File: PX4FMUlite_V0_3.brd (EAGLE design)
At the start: 48.6 x 34.9 mm, 151 parts, among them J2 DF13-4P-1.25V, J201 DF13C-6P-1.25V, J202 DF13C-6P-1.25V, J203 DF13C-6P-1.25V, J3 DF13C-4P-1.25V, J302 DF13C-4P-1.25V, J401 DF13C-4P-1.25V, J403 DF13C-7P-1.25V, J405 DF13C-4P-1.25V, J801 JST-ZH-3, J802 DF13C-3P-1.25V, M3_MOUNT1101 MOUNT-HOLE3.1MM, M3_MOUNT1102 MOUNT-HOLE3.1MM, M3_MOUNT1103 MOUNT-HOLE3.1MM, M3_MOUNT1104 MOUNT-HOLE3.1MM, U101 STM32F4X7VX, U2 MAX3051, U401 MAX3051, U903 74LVC2G240, X101 3.2x2.5 mm / 24 MHz / 15 ppm

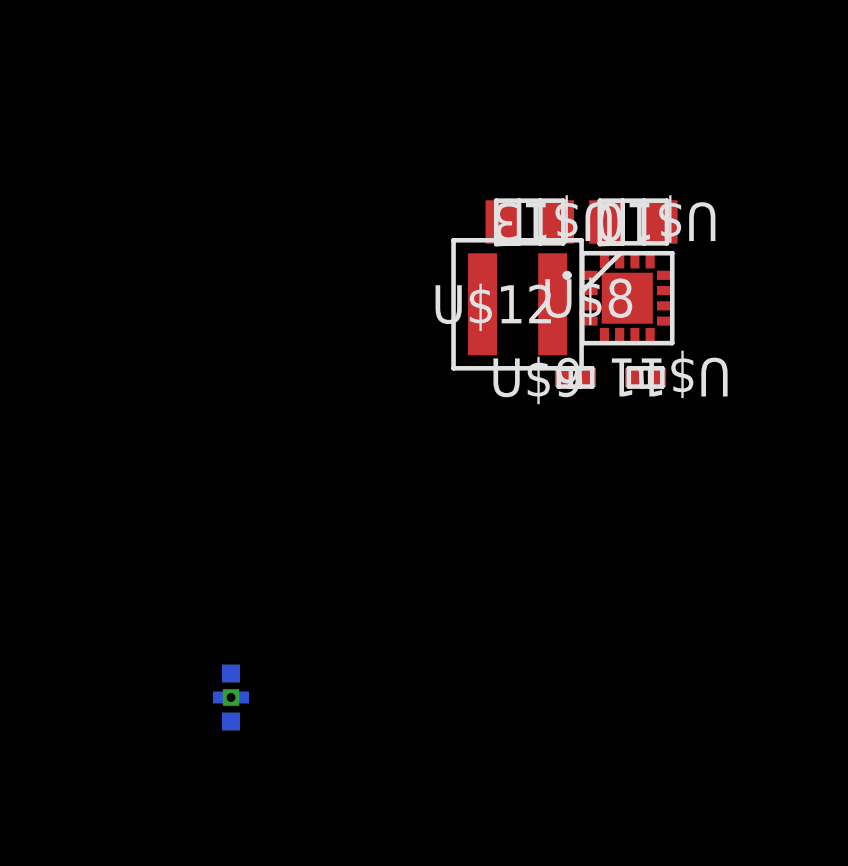
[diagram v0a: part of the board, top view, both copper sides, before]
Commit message: Added cap to TPS63031 buck-boost
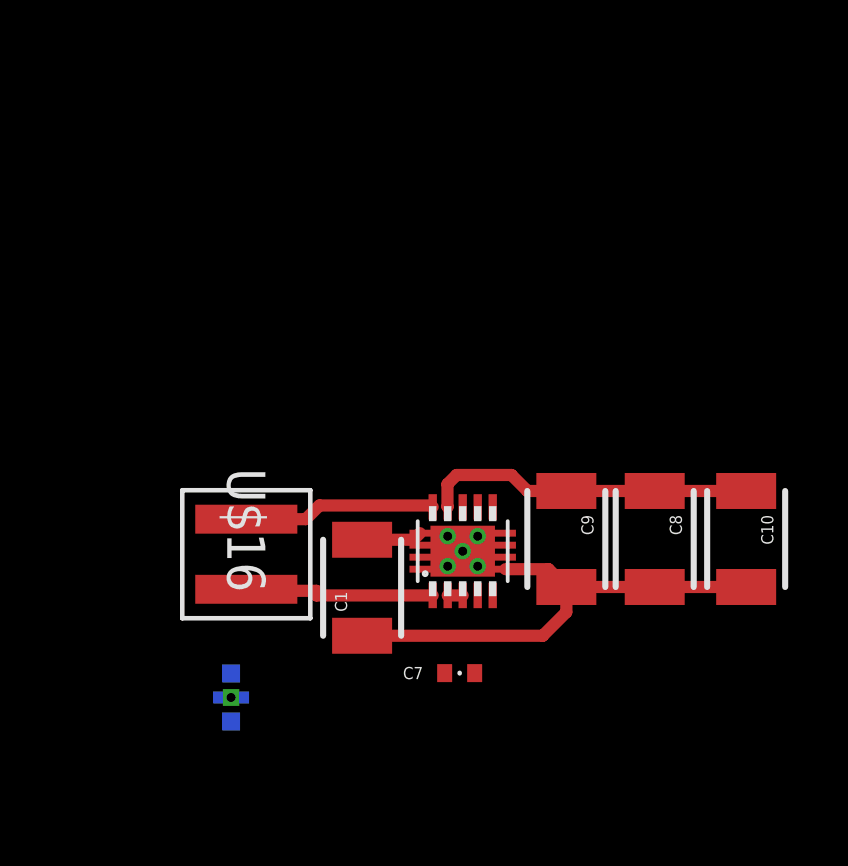
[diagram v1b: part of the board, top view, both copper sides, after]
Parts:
- removed U$10: GRM21BR61C106KE15L, ti_tps_soln2:0805
- removed U$11: GRM155R61C223KA01D, ti_tps_soln2:0402
- removed U$12: XFL4020-222MEB, ti_tps_soln2:XFL4020
- removed U$13: LMK212BJ226MG-T, ti_tps_soln2:0805
- removed U$8: TPS62143RGTR, ti_tps_soln2:S-PVQFN-N16
- removed U$9: CRCW0402100KFKED, ti_tps_soln2:0402
- added C1, C10, C8, C9: 22uF, SparkFun-Capacitors:1210
- added C7: 8p, pixhawk2:0402-CAP
- added U$15: TPS6303X, PX4lite:PWSON10
- added U$16: XFL4020-222MEB, ti_tps_soln2:XFL4020
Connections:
- removed net N$40: U$11.1, U$8.9
- new net N$10: U$15.14, U$16.1
- new net N$17: U$15.1, U$16.2
- new net VOUT: C10.1, C8.1, C9.1, U$15.13
- net !VDD_SERVO_VALID: no longer U$8.4, U$9.2
- net GND: now also U$15.11; no longer U$10.2, U$11.2, U$13.1, U$8.15, U$8.17, U$8.5, U$8.6, U$8.7, U$8.8
- net N$14: now also C1.2, C10.2, C8.2, C9.2, U$15.15, U$15.16, U$15.17, U$15.18, U$15.19, U$15.20, U$15.21, U$15.22, U$15.23, U$15.6, U$15.7, U$15.8, U$15.9, U$15.EP; no longer U$12.2, U$8.1
- net VDD_5V_IN: no longer U$12.1, U$13.2, U$8.14, U$9.1
- net VDD_IN: now also C1.1, U$15.2, U$15.3; no longer U$10.1, U$8.10, U$8.11, U$8.13
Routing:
- net N$14: track 0.00 -> 13.1 mm
- net VOUT: track 0.00 -> 11.1 mm
- net VDD_IN: track 0.00 -> 8.65 mm
- net N$10: track 0.00 -> 6.42 mm
- net N$17: track 0.00 -> 6.42 mm

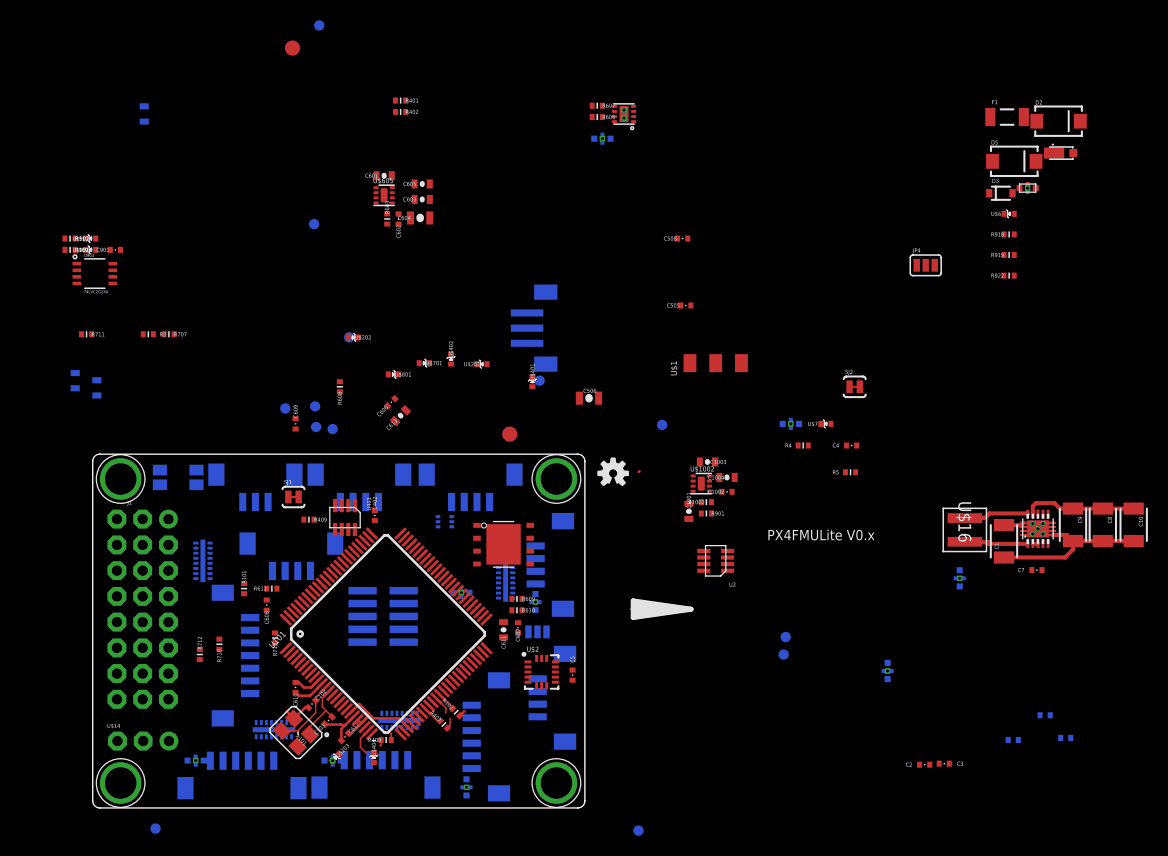
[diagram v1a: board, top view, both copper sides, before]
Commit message: Crystal rewire
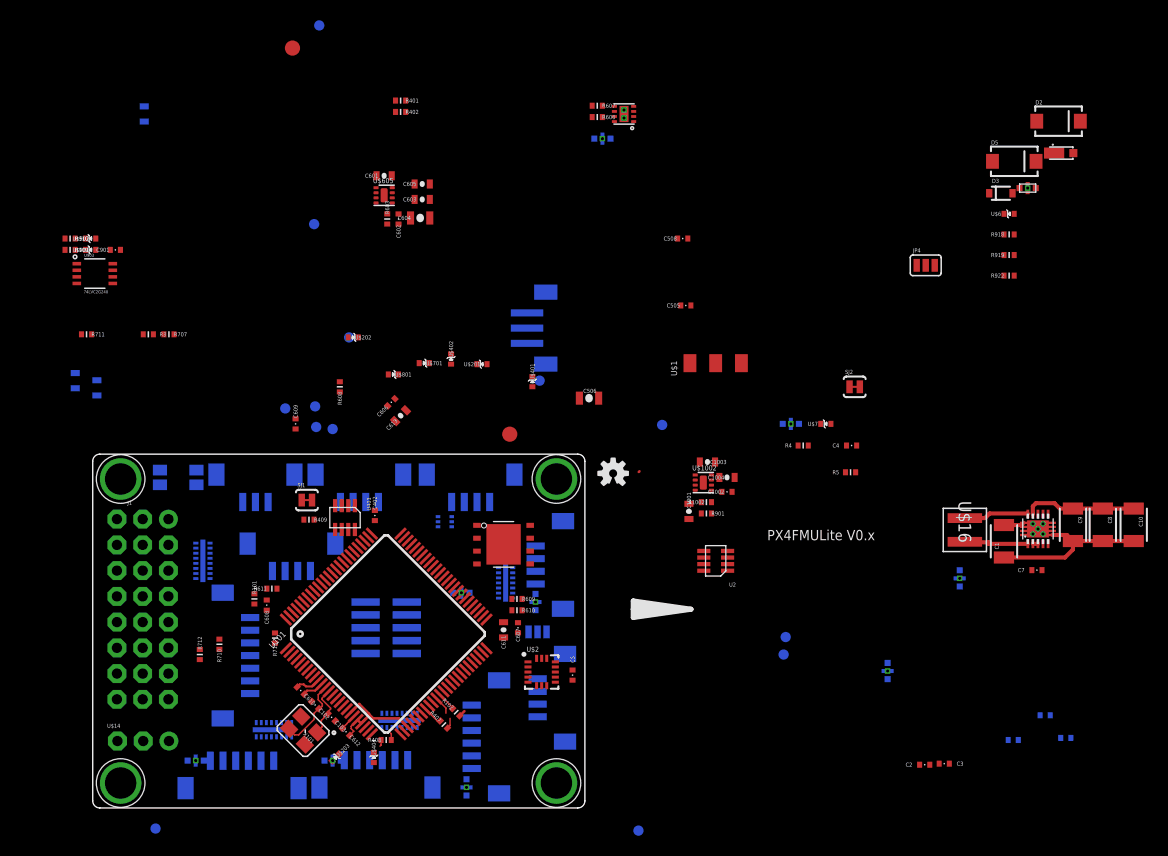
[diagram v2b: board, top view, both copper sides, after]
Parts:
- removed F1: PTCSMD-W, SparkFun-PowerIC:PTC-1206-WIDE
- moved R101 1.44 mm to (25.2, 23.4)
- moved SJ1 1.36 mm to (30.4, 33.1)
- moved JX301 1.16 mm to (38.2, 20.5)
- moved X101 0.74 mm to (30.0, 10.4)
- moved C610 0.59 mm to (29.8, 14.3), turned to 135 degrees
- moved C612 0.52 mm to (34.2, 10.3), turned to 135 degrees
- moved C103 0.43 mm to (32.8, 11.7), turned to 135 degrees
- moved C102 0.32 mm to (31.2, 12.9), turned to 135 degrees
- moved U$1002 0.23 mm to (69.5, 34.8)
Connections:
- removed net N$24: LED705.A
- net FMU-VDD_5V: now also LED705.A
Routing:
- net GND: track 11.3 -> 5.06 mm
- net FMU-UART4_RX: track 2.81 -> 0.00 mm
- net N$1: track 6.19 -> 5.47 mm
- net FMU-VDD_3V3: track 13.8 -> 13.1 mm
- net N$2: track 6.93 -> 7.51 mm

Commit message: buck-boost half wired. CAN wiring in progress.
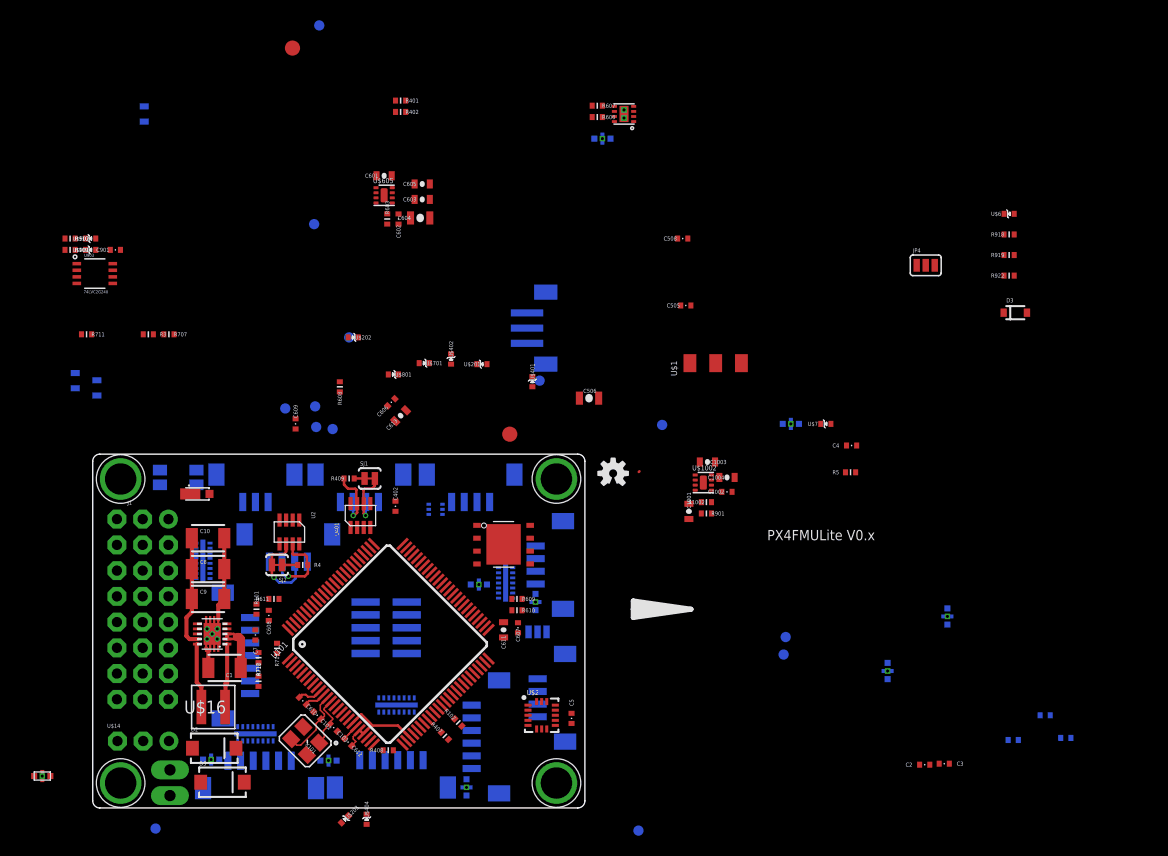
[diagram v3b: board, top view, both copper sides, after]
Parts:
- added JP5: M02PTH3, SparkFun-Connectors:1X02_LONGPADS
- moved L901 113.2 mm to (4.27, 5.89)
- moved D2 103.8 mm to (21.2, 8.64)
- moved D5 99.3 mm to (22.0, 5.28)
- moved D1 91.6 mm to (20.1, 33.7)
- moved C10 91.3 mm to (20.6, 29.4), turned to 0 degrees
- moved C8 88.4 mm to (20.6, 26.3), turned to 0 degrees
- moved C9 85.7 mm to (20.6, 23.4), turned to 0 degrees
- moved U$15 82.1 mm to (21.0, 19.9), turned to 90 degrees
- moved C1 77.9 mm to (22.3, 16.6), turned to 180 degrees
- moved C7 77.4 mm to (25.3, 19.8), turned to 90 degrees
- moved U$16 76.2 mm to (21.1, 12.7), turned to 0 degrees
- moved SJ2 59.6 mm to (27.4, 26.7), turned to 180 degrees
- moved R4 50.8 mm to (30.0, 26.7), turned to 180 degrees
- moved U2 42.2 mm to (28.7, 30.0), turned to 180 degrees
- moved D3 11.9 mm to (100.3, 51.6)
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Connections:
- net VBUS renamed V_BUS
- net VDD_SERVO renamed V_SERVO
- removed net N$14: C1.2, C10.2, C8.2, C9.2, U$15.15, U$15.16, U$15.17, U$15.18, U$15.19, U$15.20, U$15.21, U$15.22, U$15.23, U$15.6, U$15.7, U$15.8, U$15.9, U$15.EP
- removed net VBATT: D5.A
- removed net VOUT: C10.1, C8.1, C9.1, U$15.13
- new net V_EXT: D5.A, JP5.1
- net FMU-BOOT0: now also FMU-BOOT1101.P$1
- net GND: now also C1.2, C10.2, C8.2, C9.2, JP5.2, U$15.15, U$15.16, U$15.17, U$15.18, U$15.19, U$15.20, U$15.21, U$15.22, U$15.23, U$15.6, U$15.7, U$15.8, U$15.9, U$15.EP
- net GYRO_DRDY: now also U$2.9
- net VDD_5V_IN: now also C10.1, C8.1, C9.1, U$15.13
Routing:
- net N$14: track 13.1 -> 0.00 mm
- net GND: track 5.06 -> 17.5 mm
- net VOUT: track 11.1 -> 0.00 mm
- net VDD_5V_IN: track 0.00 -> 11.1 mm
- net CAN2_L: track 0.00 -> 8.74 mm, vias 0 -> 1
- net CAN2_H: track 0.00 -> 8.09 mm, vias 0 -> 1
- net CAN1_H: track 0.00 -> 6.17 mm, vias 0 -> 1
- net CAN1_L: track 0.00 -> 5.81 mm, vias 0 -> 1
- net VDD_IN: track 8.65 -> 6.14 mm
- net FMU_AUX_ADC2: track 1.93 -> 0.00 mm
- net MAG_DRDY: track 1.85 -> 0.00 mm
- net PB2-BOOT1: track 1.88 -> 0.11 mm
- net N$29: track 0.00 -> 1.53 mm
- net N$22: track 0.00 -> 1.02 mm
- net FMU_AUX_ADC2_PROT: track 1.14 -> 0.16 mm
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
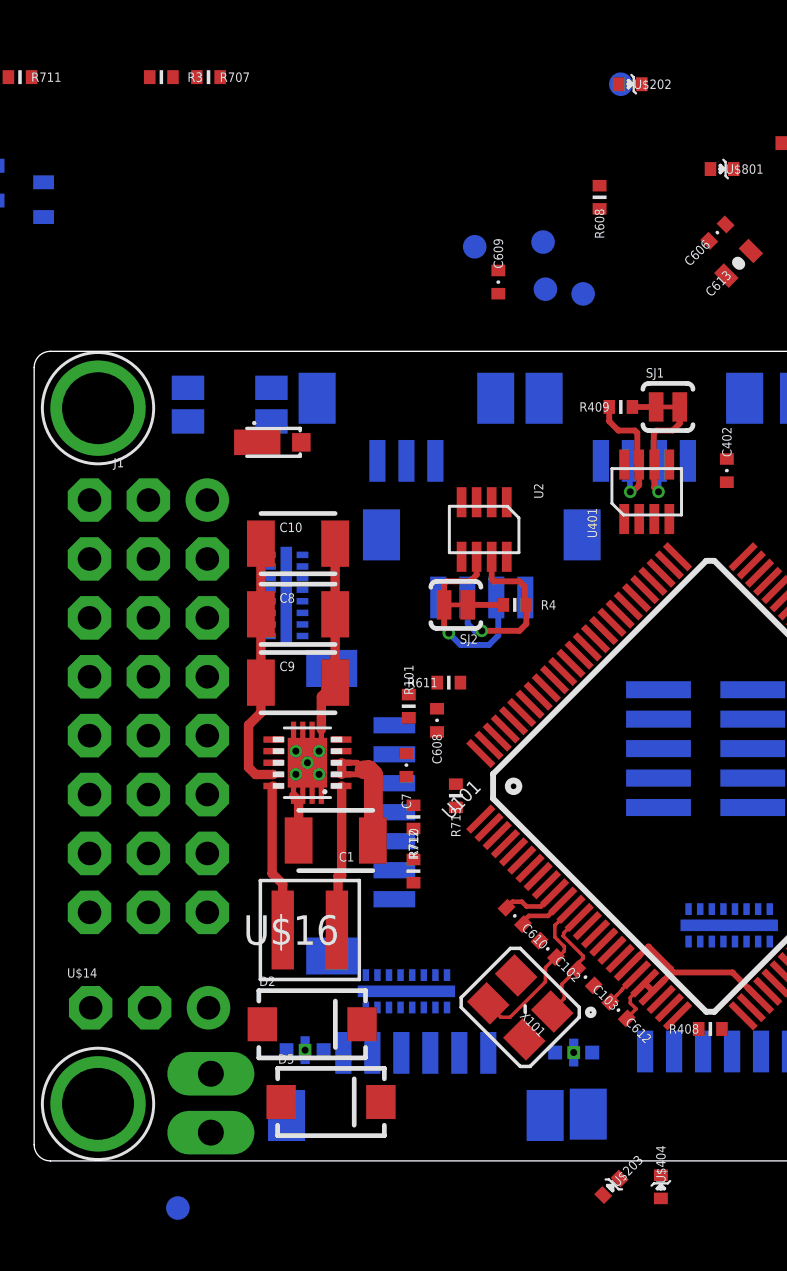
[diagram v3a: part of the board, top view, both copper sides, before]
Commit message: Adjusted servo connector direction
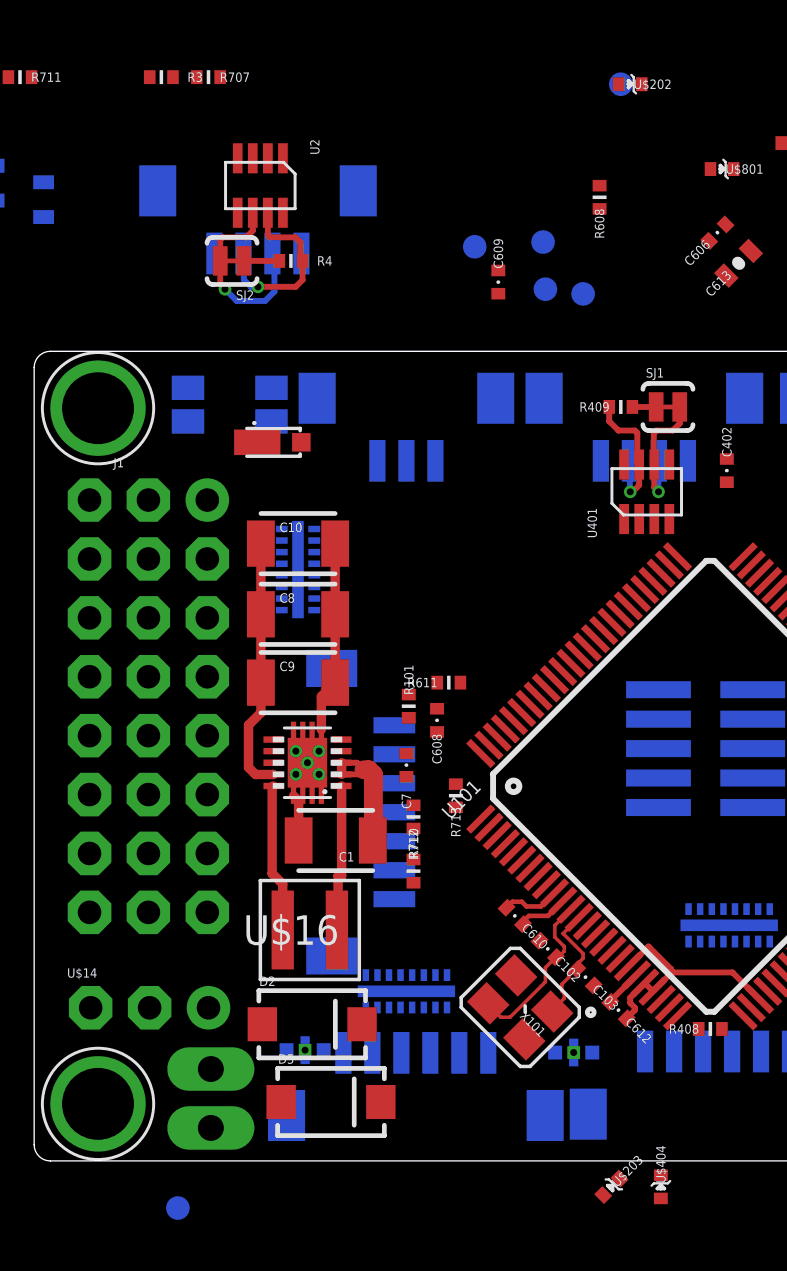
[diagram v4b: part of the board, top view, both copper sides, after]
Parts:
- moved J3 17.7 mm to (18.9, 42.8)
- moved R4 17.7 mm to (20.3, 41.6)
- moved SJ2 17.7 mm to (17.8, 41.6)
- moved U2 17.7 mm to (19.0, 44.8)
- moved L1 1.23 mm to (20.6, 28.2)
- moved JP5 0.20 mm to (16.9, 6.71)
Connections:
- net FMU-CH1-PROT: now also J1.S1; no longer J1.S8
- net N$15: now also J1.S8; no longer J1.S1
- net N$16: now also J1.S7; no longer J1.S2
- net N$36: now also J1.S6; no longer J1.S3
- net N$68: now also J1.S5; no longer J1.S4
- net N$77: now also J1.S4; no longer J1.S5
- net N$78: now also J1.S3; no longer J1.S6
- net N$79: now also J1.S2; no longer J1.S7

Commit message: More wiring done
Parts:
- removed FMU-BOOT1101: PAD.04, pixhawk2:PAD.04X.04
- added C11, C12, C6: 0u1, pixhawk2:0402-CAP
- added FMU-BOOT0: PAD.04, pixhawk2:PAD.04X.04
- added R6: 10K, pixhawk2:0402-RES
- C7: value 8p -> 0u1
- moved C4 60.0 mm to (24.4, 33.1)
- moved L202 52.0 mm to (43.4, 8.13)
- moved C1 43.1 mm to (16.8, 59.3)
- moved U$16 43.0 mm to (20.8, 55.7), turned to 90 degrees
- moved U$202 42.7 mm to (45.8, 7.92), turned to 90 degrees
- moved J403 41.3 mm to (65.0, 13.7), turned to 270 degrees
- moved U$15 36.0 mm to (16.8, 55.7), turned to 180 degrees
- moved C7 34.5 mm to (16.4, 53.1), turned to 180 degrees
- moved D1 31.8 mm to (31.5, 63.4), turned to 270 degrees
- moved L403 29.6 mm to (72.5, 18.2)
- moved C9 28.0 mm to (16.9, 51.1), turned to 180 degrees
- moved C8 22.2 mm to (16.9, 48.2), turned to 180 degrees
- moved J802 17.8 mm to (29.1, 51.2)
- moved L201 16.7 mm to (48.5, 12.2), turned to 90 degrees
- moved C10 16.3 mm to (16.9, 45.2), turned to 180 degrees
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- renumbered VDDA_3V1101 to VDDA_3V3_SENSORS, VDD_3V1101 to VDD_3V3
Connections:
- net N$100 renamed 5V_S3_FILTERED
- net N$101 renamed 5V_S2_FILTERED
- net N$5 renamed 5V_S1_FILTERED
- removed net VDD_5V_HIPOWER: L201.P$1
- removed net VDD_5V_IN: C10.1, C8.1, C9.1, L603.P$1, R609.P$2, U$15.13, U$604.1
- new net !VDD_5V_VALID: R6.P$1, U$15.5
- new net N$27: C6.P$1, U$15.10
- new net VDD_5V: C10.1, C11.P$1, C7.P$1, C8.1, C9.1, L603.P$1, R6.P$2, R609.P$2, U$15.13, U$604.1
- net FMU-BOOT0: now also FMU-BOOT0.P$1; no longer FMU-BOOT1101.P$1
- net GND: now also C11.P$2, C12.P$2, C6.P$2, C7.P$2, U$15.4
- net VDD_5V_PERIPH: now also L201.P$1
- net VDD_IN: now also C12.P$1
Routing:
- net GND: track 17.5 -> 42.3 mm
- net 5V_S3_FILTERED: track 0.00 -> 15.9 mm
- net N$15: track 0.00 -> 15.9 mm
- net N$16: track 0.00 -> 14.0 mm
- net N$36: track 0.00 -> 12.2 mm
- net VDD_5V_IN: track 11.1 -> 0.00 mm
- net N$68: track 0.00 -> 10.2 mm
- net VDD_5V: track 0.00 -> 10.1 mm
- net N$77: track 0.00 -> 8.39 mm
- net N$78: track 0.00 -> 6.47 mm
- net FMU-VDD_3V3: track 13.1 -> 18.4 mm
- net CAN1_H: track 6.17 -> 10.8 mm, vias 1 -> 2
- net V_EXT: track 0.00 -> 4.51 mm
- net N$79: track 0.00 -> 4.49 mm
- net FMU-CH1-PROT: track 0.00 -> 4.20 mm
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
